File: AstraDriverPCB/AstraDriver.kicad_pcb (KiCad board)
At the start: 4 copper layers, 102 x 96 mm, 98 parts, among them CN1 JST VH 8 PIN, CN2 JST VH 2 PIN, CN3 JST VH 2 PIN, CN4 JST VH 2 PIN, CN5 JST VH 2 PIN, U1 LED2001PHR, U2 LED2001PHR, U3 LED2001PHR, U4 LED2001PHR

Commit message: Tweak angled render
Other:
- board text added: "M5"

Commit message: New layout in progress
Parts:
- removed C15: DNP, LiveAstra:C_DNP_0805_2012Metric_Pad1.18x1.45mm_HandSolder
- removed C16: 22u, LiveAstra:C_0805_2012Metric_Pad1.18x1.45mm_HandSolder
- removed C17, C18: 1u, LiveAstra:C_0805_2012Metric_Pad1.18x1.45mm_HandSolder
- added C19: 10n, LiveAstra:C_0805_2012Metric_Pad1.18x1.45mm_HandSolder, F.Cu at (146.0, 62.2)
- added C20: 10n, LiveAstra:C_0805_2012Metric_Pad1.18x1.45mm_HandSolder, F.Cu at (146.0, 147.8)
- added C21: 10n, LiveAstra:C_0805_2012Metric_Pad1.18x1.45mm_HandSolder, F.Cu at (194.2, 90.2)
- added C22: 10n, LiveAstra:C_0805_2012Metric_Pad1.18x1.45mm_HandSolder, F.Cu at (102.5, 90.2)
- added R11: 1M, LiveAstra:R_0805_2012Metric_Pad1.20x1.40mm_HandSolder, F.Cu at (151.0, 62.2)
- added R12: DNP, LiveAstra:R_DNP_0805_2012Metric_Pad1.20x1.40mm_HandSolder, F.Cu at (151.0, 147.8)
- added R13: DNP, LiveAstra:R_DNP_0805_2012Metric_Pad1.20x1.40mm_HandSolder, F.Cu at (194.2, 85.2)
- added R14: DNP, LiveAstra:R_DNP_0805_2012Metric_Pad1.20x1.40mm_HandSolder, F.Cu at (102.5, 85.2)
- added R15: 10k, LiveAstra:R_0805_2012Metric_Pad1.20x1.40mm_HandSolder, F.Cu at (160.8, 78.8)
- added R16: 10k, LiveAstra:R_0805_2012Metric_Pad1.20x1.40mm_HandSolder, F.Cu at (154.5, 78.8)
- added R17: 10k, LiveAstra:R_0805_2012Metric_Pad1.20x1.40mm_HandSolder, F.Cu at (136.5, 78.8)
- added R18: 10k, LiveAstra:R_0805_2012Metric_Pad1.20x1.40mm_HandSolder, F.Cu at (142.5, 78.8)
- added R19: 10k, LiveAstra:R_0805_2012Metric_Pad1.20x1.40mm_HandSolder, F.Cu at (148.5, 78.8)
- C10, C14, C6: value 1u -> 4u7; footprint LiveAstra:C_0805_2012Metric_Pad1.18x1.45mm_HandSolder -> LiveAstra:C_1206_3216Metric_Pad1.33x1.80mm_HandSolder
- C11: value DNP -> 4u7; footprint LiveAstra:C_DNP_0805_2012Metric_Pad1.18x1.45mm_HandSolder -> LiveAstra:C_1206_3216Metric_Pad1.33x1.80mm_HandSolder
- C12, C4, C8: footprint LiveAstra:C_0805_2012Metric_Pad1.18x1.45mm_HandSolder -> LiveAstra:C_1206_3216Metric_Pad1.33x1.80mm_HandSolder
- C3: value DNP -> 22u; footprint LiveAstra:C_DNP_0805_2012Metric_Pad1.18x1.45mm_HandSolder -> LiveAstra:C_1206_3216Metric_Pad1.33x1.80mm_HandSolder
- C7: value DNP -> 1u; footprint LiveAstra:C_DNP_0805_2012Metric_Pad1.18x1.45mm_HandSolder -> LiveAstra:C_0805_2012Metric_Pad1.18x1.45mm_HandSolder
- L1, L2, L3, L4: value 4u7H -> 2u2H; footprint LiveAstra:L_Sunlord_SWPA6045S -> LiveAstra:L_TDK_SPM6530T-2R2M
- moved L4 96.1 mm to (211.7, 106.0), turned to 0 degrees
- moved R9 96.1 mm to (236.0, 84.8), turned to 0 degrees
- moved L3 95.5 mm to (228.3, 88.6), turned to 0 degrees
- moved C11 95.5 mm to (237.2, 99.8)
- moved U4 87.4 mm to (211.6, 114.2), turned to 0 degrees
- moved U3 86.6 mm to (228.2, 96.7), turned to 0 degrees
- moved C14 84.6 mm to (218.5, 115.0), turned to 0 degrees
- moved C10 83.8 mm to (236.0, 107.5), turned to 0 degrees
- moved C12 79.9 mm to (221.0, 112.5)
- moved C13 79.8 mm to (218.5, 102.5)
- moved C7 76.9 mm to (236.0, 90.0)
- moved L2 76.7 mm to (228.3, 106.0), turned to 0 degrees
- moved C8 76.3 mm to (236.0, 102.5)
- moved C3 58.4 mm to (236.0, 95.0)
- moved C5 2.67 mm to (174.5, 110.8), turned to -90 degrees
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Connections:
- net /Block Diagram/Channel 1 2.5A/SW_OUT renamed /Block Diagram/Channel 1 Blue and CY 2.5A/SW_OUT
- net /Block Diagram/Channel 2 2.5A/SW_OUT renamed /Block Diagram/Channel 2 Blue and CY 2.5A/SW_OUT
- net /Block Diagram/Channel 3 2.5A/SW_OUT renamed /Block Diagram/Channel 3 Green 2.5A/SW_OUT
- net /Block Diagram/Channel 4 2A/SW_OUT renamed /Block Diagram/Channel 4 Red 2A/SW_OUT
- C11 pad 2: +5V -> /Block Diagram/CH3_LED+
- C14 pad 2: /Block Diagram/CH3_LED+ -> /Block Diagram/CH4_LED+
- RING1 pad 1: GND -> CHASSIS
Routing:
- net /Block Diagram/DIM_1: track 52.6 -> 19.9 mm
- net /Block Diagram/DIM_4: track 50.3 -> 35.0 mm
- net /Block Diagram/DIM_3: track 42.7 -> 35.6 mm
- net /Block Diagram/DIM_2: track 43.5 -> 36.8 mm
- net GND: track 0.00 -> 6.25 mm, vias 271 -> 145
- net +5V: track 18.1 -> 13.6 mm, vias 24 -> 34
- net /Block Diagram/RSRV: track 14.1 -> 18.1 mm
- net +3V3: track 7.55 -> 9.80 mm
- net /Block Diagram/Channel 4 Red 2A/SW_OUT: vias 12 -> 0
- net /Block Diagram/Channel 3 Green 2.5A/SW_OUT: vias 12 -> 0
- net /Block Diagram/Channel 1 Blue and CY 2.5A/SW_OUT: vias 12 -> 8
- net (no net): vias 0 -> 24
- added copper zone on B.Cu, net (none)
- added copper zone on F.Cu, net (none)
- added copper zone on F.Cu, net CHASSIS
- removed copper zone on B.Cu, net /Block Diagram/Channel 3 Green 2.5A/SW_OUT
- removed copper zone on F.Cu, net /Block Diagram/Channel 3 Green 2.5A/SW_OUT
- removed copper zone on B.Cu, net /Block Diagram/Channel 4 Red 2A/SW_OUT
- removed copper zone on F.Cu, net /Block Diagram/Channel 4 Red 2A/SW_OUT

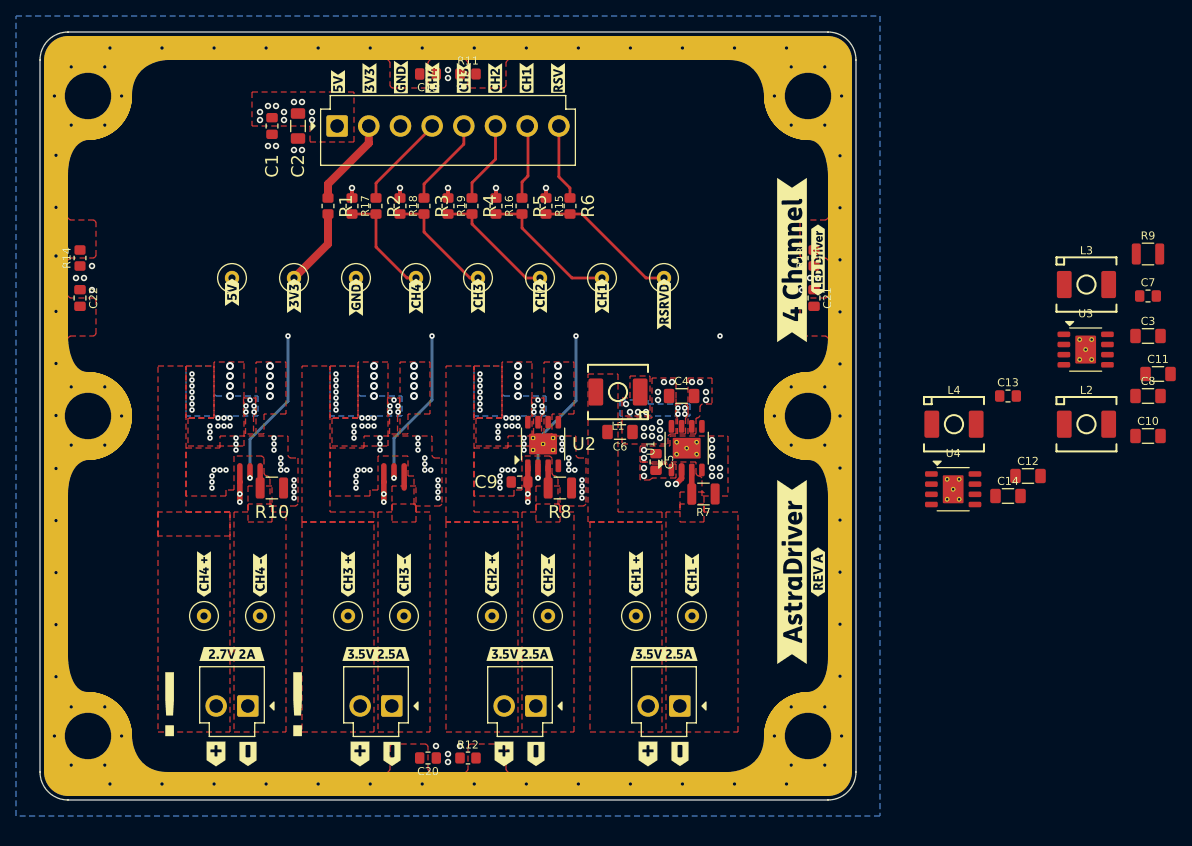
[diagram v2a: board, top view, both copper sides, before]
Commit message: Finished layout and silkscreen, and stitching
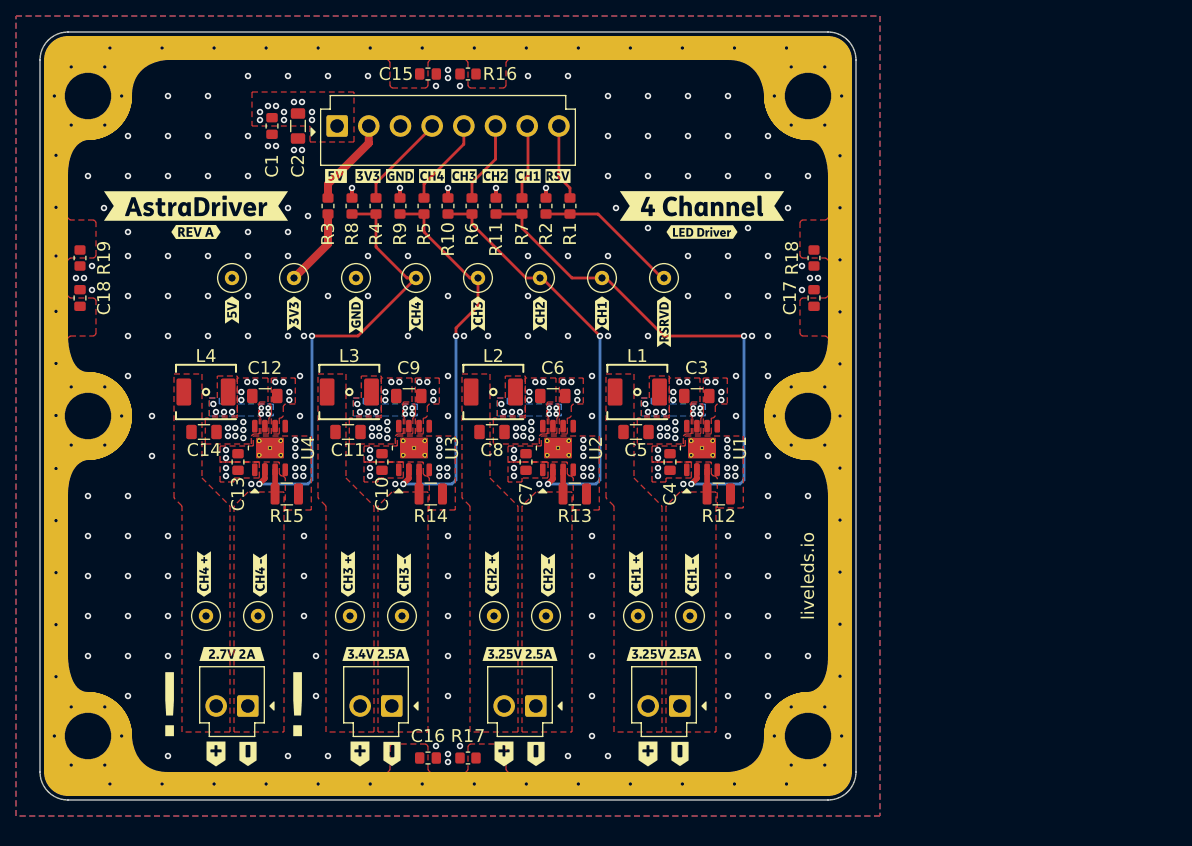
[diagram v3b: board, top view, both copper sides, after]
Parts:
- removed the C9 at (157.4, 113.2)
- removed the R10 at (126.5, 114.0)
- removed the R8 at (162.5, 114.0)
- removed kibuzzard-67263D4A: G***, kibuzzard-67263D4A
- removed kibuzzard-67263D55: G***, kibuzzard-67263D55
- removed kibuzzard-67263D65: G***, kibuzzard-67263D65
- removed kibuzzard-67263D6B: G***, kibuzzard-67263D6B
- removed kibuzzard-67263D70: G***, kibuzzard-67263D70
- removed kibuzzard-67263D73: G***, kibuzzard-67263D73
- removed kibuzzard-67263D79: G***, kibuzzard-67263D79
- removed kibuzzard-67263D89: G***, kibuzzard-67263D89
- removed kibuzzard-6726481C (x3): G***, kibuzzard-6726481C
- added C7: 1u, LiveAstra:C_0805_2012Metric_Pad1.18x1.45mm_HandSolder, F.Cu at (158.2, 110.8)
- added R13: 40m, LiveAstra:R_1210_3225Metric, F.Cu at (164.3, 114.8)
- added R15: 47m, LiveAstra:R_1210_3225Metric, F.Cu at (128.3, 114.8)
- added kibuzzard-676095B5: G***, kibuzzard-676095B5, F.Cu at (154.4, 75.0)
- added kibuzzard-676095BC: G***, kibuzzard-676095BC, F.Cu at (150.5, 75.0)
- added kibuzzard-676095C8: G***, kibuzzard-676095C8, F.Cu at (146.5, 75.0)
- added kibuzzard-676095D3: G***, kibuzzard-676095D3, F.Cu at (158.5, 75.0)
- added kibuzzard-6760963B: G***, kibuzzard-6760963B, F.Cu at (142.5, 75.0)
- added kibuzzard-67609643: G***, kibuzzard-67609643, F.Cu at (138.5, 75.0)
- added kibuzzard-6760964A: G***, kibuzzard-6760964A, F.Cu at (134.5, 75.0)
- added kibuzzard-67609673: G***, kibuzzard-67609673, F.Cu at (162.2, 75.0)
- added kibuzzard-67609A4F: G***, kibuzzard-67609A4F, F.Cu at (175.5, 134.8)
- added kibuzzard-67609A54: G***, kibuzzard-67609A54, F.Cu at (157.5, 134.8)
- added kibuzzard-67609A62: G***, kibuzzard-67609A62, F.Cu at (139.5, 134.8)
- moved C11 101.5 mm to (136.0, 107.0), turned to 180 degrees
- moved C14 100.8 mm to (118.0, 107.0), turned to 180 degrees
- moved C10 98.0 mm to (140.2, 110.8), turned to -90 degrees
- moved C13 96.6 mm to (122.2, 110.8), turned to -90 degrees
- moved C12 95.9 mm to (125.6, 102.5)
- moved R14 94.5 mm to (146.3, 114.8), turned to 180 degrees
- moved L4 93.6 mm to (118.2, 102.0), turned to 180 degrees
- moved L3 93.1 mm to (136.2, 102.0), turned to 180 degrees
- moved C9 92.7 mm to (143.6, 102.5)
- moved kibuzzard-67264F60 88.6 mm to (117.0, 82.0), turned to 0 degrees
- moved kibuzzard-67264EAC 87.4 mm to (117.0, 78.8), turned to 0 degrees
- moved U4 85.6 mm to (126.2, 109.0), turned to 90 degrees
- moved U3 84.9 mm to (144.2, 109.0), turned to 90 degrees
- moved C8 82.0 mm to (154.0, 107.0), turned to 180 degrees
- moved C6 74.4 mm to (161.6, 102.5)
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- renumbered C7 to C10, C19 to C15, C20 to C16, C21 to C17, C22 to C18, C4 to C3, C5 to C4, C6 to C5, C8 to C6, C10 to C8, C3 to C9, R6 to R1, R19 to R10, R16 to R11, R7 to R12, R9 to R14, R11 to R16, R12 to R17, R13 to R18, R14 to R19, R15 to R2, R1 to R3, R2 to R4, R3 to R5, R4 to R6, R5 to R7, R17 to R8, R18 to R9, TP3 to TP1, TP8 to TP2, TP1 to TP3, TP2 to TP4, TP4 to TP5, TP5 to TP6, TP6 to TP7, TP7 to TP8
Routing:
- net /Block Diagram/DIM_1: track 19.9 -> 65.5 mm
- net /Block Diagram/DIM_4: track 35.0 -> 57.1 mm
- net /Block Diagram/DIM_2: track 36.8 -> 52.8 mm
- net /Block Diagram/DIM_3: track 35.6 -> 50.2 mm
- net +5V: track 13.6 -> 0.00 mm
- net GND: vias 145 -> 253
- net /Block Diagram/Channel 4 Red 2A/SW_OUT: vias 0 -> 8
- net /Block Diagram/Channel 3 Green 2.5A/SW_OUT: vias 0 -> 8
- net /Block Diagram/Channel 2 Blue and CY 2.5A/SW_OUT: vias 12 -> 8
- net (no net): vias 24 -> 0
- added copper zone on B.Cu, net /Block Diagram/Channel 3 Green 2.5A/SW_OUT
- added copper zone on F.Cu, net /Block Diagram/Channel 3 Green 2.5A/SW_OUT
- added copper zone on B.Cu, net /Block Diagram/Channel 4 Red 2A/SW_OUT
- added copper zone on F.Cu, net /Block Diagram/Channel 4 Red 2A/SW_OUT
- removed copper zone on B.Cu, net (none)
- removed copper zone on F.Cu, net (none)
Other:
- board text added: "liveleds.io"

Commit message: Prepare for review, cleanup
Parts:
- added kibuzzard-6762FA53: G***, kibuzzard-6762FA53, F.Cu at (193.5, 124.5)
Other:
- board text removed: "liveleds.io"
